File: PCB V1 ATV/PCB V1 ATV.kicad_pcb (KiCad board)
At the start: 2 copper layers, 101.6 x 53.3 mm, 25 parts, among them J1 Power, J10 NW Sensor, J11 N Sensor, J12 NE Sensor, J13 SW Sensor, J14 S Sensor, J15 SE Sensor, J16 Joystick, J17 MotorControl, J2 PWM, J3 Analog, J4 PWM, J5 Analog, J6 Communication, J7 Digital, J8 Battery 12vIN, J9 Motor Controller, SW1 EStop, U1 L7809

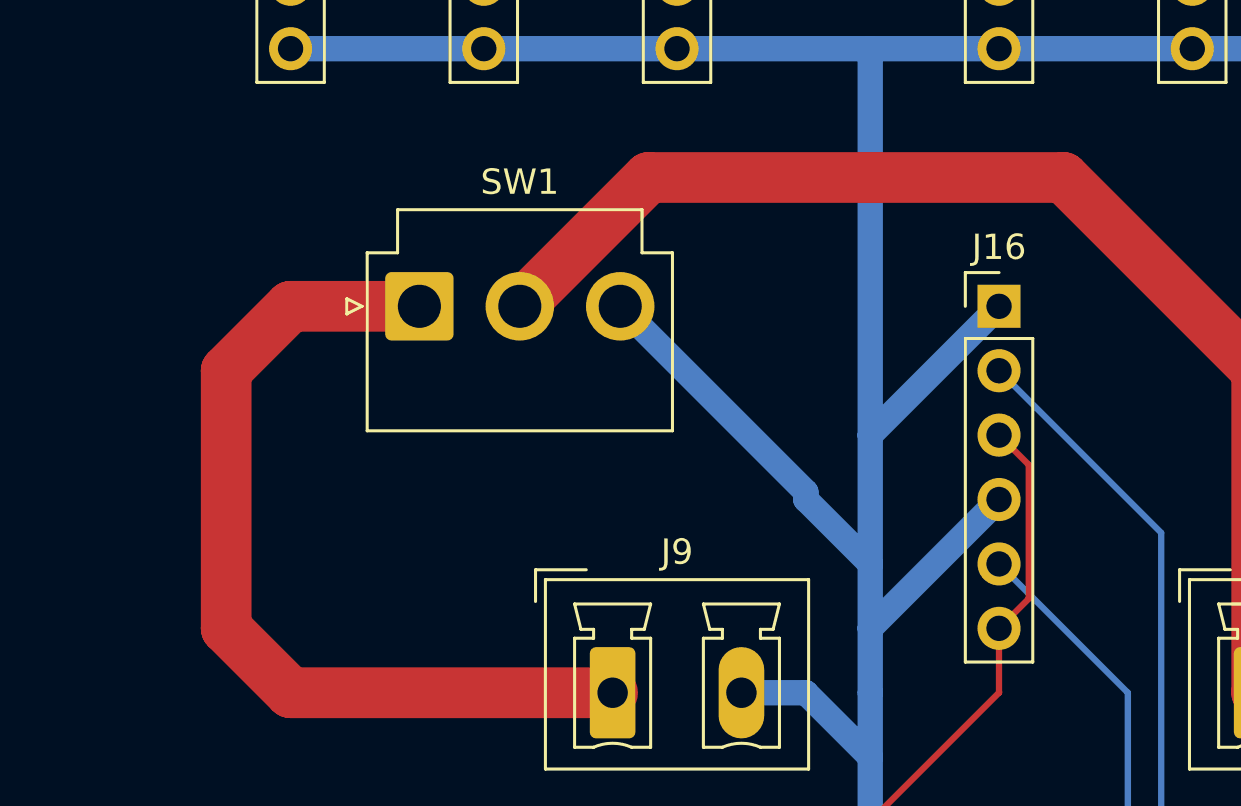
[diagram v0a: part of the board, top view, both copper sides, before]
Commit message: V2.0
Added resistor between estop and ground
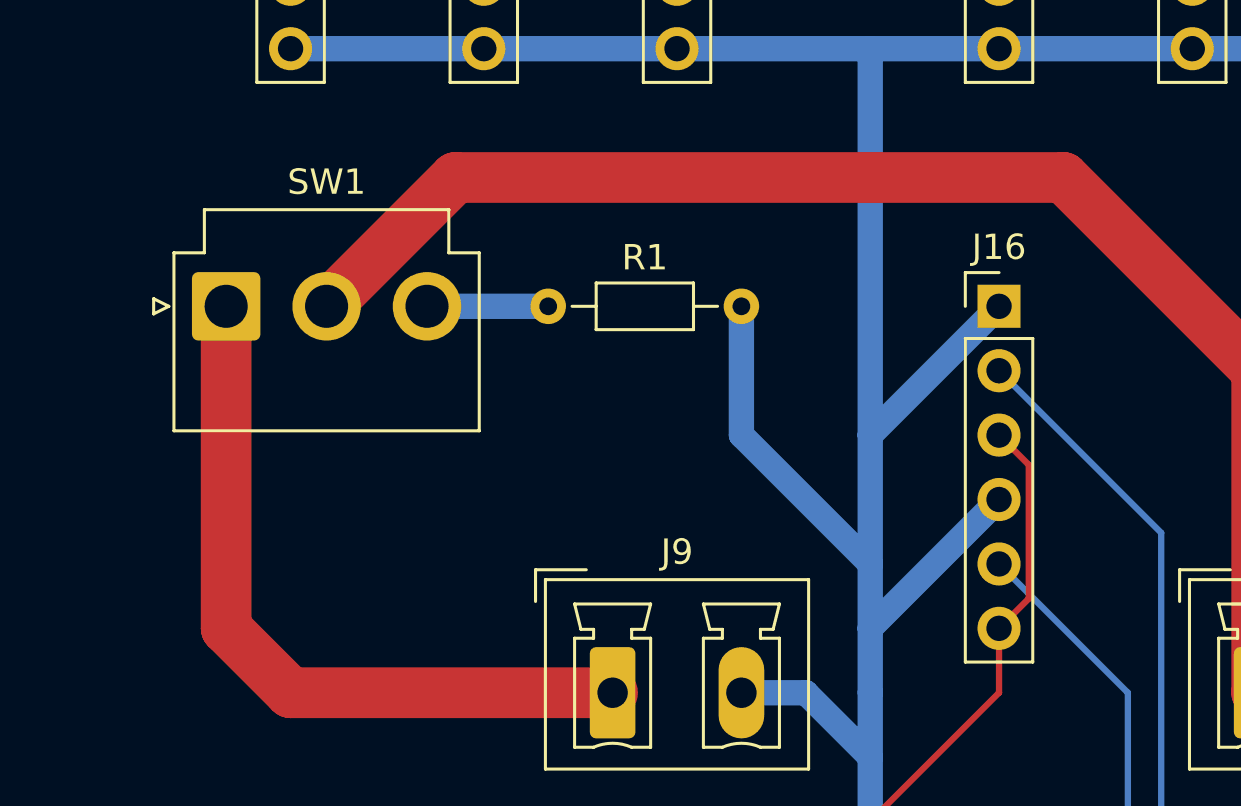
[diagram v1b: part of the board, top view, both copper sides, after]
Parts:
- added R1: R, Resistor_THT:R_Axial_DIN0204_L3.6mm_D1.6mm_P7.62mm_Horizontal, F.Cu at (127.9, 74.6)
- moved SW1 7.62 mm to (115.2, 74.6)
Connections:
- SW1 pad 3: GND -> Net-(SW1A-C)
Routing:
- net Net-(J8-Pin_1): track 70.5 -> 78.1 mm
- net Net-(J9-Pin_1): track 35.1 -> 29.0 mm
- net Net-(SW1A-C): track 0.00 -> 4.78 mm
- net GND: track 162.4 -> 160.4 mm
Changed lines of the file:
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@@
   (net 79 "VCC")
   (net 80 "Net-(J9-Pin_1)")
+  (net 81 "Net-(SW1A-C)")
   (footprint "Connector_PinSocket_2.54mm:PinSocket_2x18_P2.54mm_Vertical" locked (layer "F.Cu")
     (at 193.98 92.38 180)
@@
     (pad "" np_thru_hole circle locked (at 0 0) (size 3.2 3.2) (drill 3.2) (layers "*.Cu" "*.Mask"))
   )
+  (footprint "Resistor_THT:R_Axial_DIN0204_L3.6mm_D1.6mm_P7.62mm_Horizontal" (layer "F.Cu")
+    (at 127.94 74.6)
+    (descr "Resistor, Axial_DIN0204 series, Axial, Horizontal, pin pitch=7.62mm, 0.167W, length*diameter=3.6*1.6mm^2, http://cdn-reichelt.de/documents/datenblatt/B400/1_4W%23YAG.pdf")
+    (tags "Resistor Axial_DIN0204 series Axial Horizontal pin pitch 7.62mm 0.167W length 3.6mm diameter 1.6mm")
+    (property "Sheetfile" "PCB V1 ATV.kicad_sch")
+    (property "Sheetname" "")
+    (property "ki_description" "Resistor")
+    (property "ki_keywords" "R res resistor")
+    (attr through_hole)
+    (fp_text reference "R1" (at 3.81 -1.92) (layer "F.SilkS")
+        (effects (font (size 1 1) (thickness 0.15)))
+    )
+    (fp_text value "R" (at 3.81 1.92) (layer "F.Fab")
+        (effects (font (size 1 1) (thickness 0.15)))
+    )
+    (fp_text user "${REFERENCE}" (at 3.81 0) (layer "F.Fab")
+        (effects (font (size 0.72 0.72) (thickness 0.108)))
+    )
+    (fp_line (start 0.94 0) (end 1.89 0)
+      (stroke (width 0.12) (type solid)) (layer "F.SilkS"))
+    (fp_line (start 1.89 -0.92) (end 1.89 0.92)
+      (stroke (width 0.12) (type solid)) (layer "F.SilkS"))
+    (fp_line (start 1.89 0.92) (end 5.73 0.92)
+      (stroke (width 0.12) (type solid)) (layer "F.SilkS"))
+    (fp_line (start 5.73 -0.92) (end 1.89 -0.92)
+      (stroke (width 0.12) (type solid)) (layer "F.SilkS"))
+    (fp_line (start 5.73 0.92) (end 5.73 -0.92)
+      (stroke (width 0.12) (type solid)) (layer "F.SilkS"))
+    (fp_line (start 6.68 0) (end 5.73 0)
+      (stroke (width 0.12) (type solid)) (layer "F.SilkS"))
+    (fp_line (start -0.95 -1.05) (end -0.95 1.05)
+      (stroke (width 0.05) (type solid)) (layer "F.CrtYd"))
+    (fp_line (start -0.95 1.05) (end 8.57 1.05)
+      (stroke (width 0.05) (type solid)) (layer "F.CrtYd"))
+    (fp_line (start 8.57 -1.05) (end -0.95 -1.05)
+      (stroke (width 0.05) (type solid)) (layer "F.CrtYd"))
+    (fp_line (start 8.57 1.05) (end 8.57 -1.05)
+      (stroke (width 0.05) (type solid)) (layer "F.CrtYd"))
+    (fp_line (start 0 0) (end 2.01 0)
+      (stroke (width 0.1) (type solid)) (layer "F.Fab"))
+    (fp_line (start 2.01 -0.8) (end 2.01 0.8)
+      (stroke (width 0.1) (type solid)) (layer "F.Fab"))
+    (fp_line (start 2.01 0.8) (end 5.61 0.8)
+      (stroke (width 0.1) (type solid)) (layer "F.Fab"))
+    (fp_line (start 5.61 -0.8) (end 2.01 -0.8)
+      (stroke (width 0.1) (type solid)) (layer "F.Fab"))
+    (fp_line (start 5.61 0.8) (end 5.61 -0.8)
+      (stroke (width 0.1) (type solid)) (layer "F.Fab"))
+    (fp_line (start 7.62 0) (end 5.61 0)
+      (stroke (width 0.1) (type solid)) (layer "F.Fab"))
+    (pad "1" thru_hole circle (at 0 0) (size 1.4 1.4) (drill 0.7) (layers "*.Cu" "*.Mask")
+      (net 81 "Net-(SW1A-C)") (pintype "passive"))
+    (pad "2" thru_hole oval (at 7.62 0) (size 1.4 1.4) (drill 0.7) (layers "*.Cu" "*.Mask")
+      (net 1 "GND") (pintype "passive"))
+    (model "${KICAD6_3DMODEL_DIR}/Resistor_THT.3dshapes/R_Axial_DIN0204_L3.6mm_D1.6mm_P7.62mm_Horizontal.wrl"
+      (offset (xyz 0 0 0))
+      (scale (xyz 1 1 1))
+      (rotate (xyz 0 0 0))
+    )
+  )
   (footprint "Connector_Phoenix_MC_HighVoltage:PhoenixContact_MCV_1,5_2-G-5.08_1x02_P5.08mm_Vertical" (layer "F.Cu")
     (at 130.48 89.84)
@@
   )
   (footprint "Connector_JST:JST_VH_B3P-VH-B_1x03_P3.96mm_Vertical" (layer "F.Cu")
-    (at 122.86 74.6)
+    (at 115.24 74.6)
     (descr "JST VH PBT series connector, B3P-VH-B (http://www.jst-mfg.com/product/pdf/eng/eVH.pdf), generated with kicad-footprint-generator")
     (tags "connector JST VH vertical")
@@
       (net 78 "Net-(J8-Pin_1)") (pinfunction "B") (pintype "passive"))
     (pad "3" thru_hole circle (at 7.92 0) (size 2.7 2.7) (drill 1.7) (layers "*.Cu" "*.Mask")
-      (net 1 "GND") (pinfunction "C") (pintype "passive"))
+      (net 81 "Net-(SW1A-C)") (pinfunction "C") (pintype "passive"))
     (model "${KICAD6_3DMODEL_DIR}/Connector_JST.3dshapes/JST_VH_B3P-VH-B_1x03_P3.96mm_Vertical.wrl"
       (offset (xyz 0 0 0))
@@
   (segment (start 140.64 89.84) (end 140.64 97.46) (width 1) (layer "B.Cu") (net 1))
   (segment (start 158.42 84.76) (end 160.96 87.3) (width 1) (layer "B.Cu") (net 1))
-  (segment (start 138.1 82.22) (end 138.1 81.92) (width 1) (layer "B.Cu") (net 1))
   (segment (start 193.98 92.38) (end 196.52 92.38) (width 1) (layer "B.Cu") (net 1))
-  (segment (start 138.1 81.92) (end 130.78 74.6) (width 1) (layer "B.Cu") (net 1))
+  (segment (start 135.56 74.6) (end 135.56 79.68) (width 1) (layer "B.Cu") (net 1))
   (segment (start 140.64 84.76) (end 140.64 79.68) (width 1) (layer "B.Cu") (net 1))
   (segment (start 140.64 89.84) (end 140.64 87.3) (width 1) (layer "B.Cu") (net 1))
@@
   (segment (start 140.64 79.68) (end 140.64 64.44) (width 1) (layer "B.Cu") (net 1))
   (segment (start 145.72 64.44) (end 153.34 64.44) (width 1) (layer "B.Cu") (net 1))
+  (segment (start 135.56 79.68) (end 140.64 84.76) (width 1) (layer "B.Cu") (net 1))
   (segment (start 158.42 64.44) (end 158.42 84.76) (width 1) (layer "B.Cu") (net 1))
   (segment (start 140.64 87.3) (end 145.72 82.22) (width 1) (layer "B.Cu") (net 1))
@@
   (segment (start 178.74 82.22) (end 178.74 87.3) (width 1) (layer "B.Cu") (net 1))
   (segment (start 140.64 79.68) (end 145.72 74.6) (width 1) (layer "B.Cu") (net 1))
-  (segment (start 138.1 82.22) (end 140.64 84.76) (width 1) (layer "B.Cu") (net 1))
   (segment (start 158.42 64.44) (end 160.96 64.44) (width 1) (layer "B.Cu") (net 1))
   (segment (start 117.78 64.44) (end 125.4 64.44) (width 1) (layer "B.Cu") (net 1))
@@
   (segment (start 163.5 59.36) (end 163.5 54.28) (width 0.25) (layer "B.Cu") (net 64))
   (segment (start 155.88 89.84) (end 163.5 82.22) (width 2) (layer "F.Cu") (net 78))
-  (segment (start 148.26 69.52) (end 131.9 69.52) (width 2) (layer "F.Cu") (net 78))
+  (segment (start 155.88 89.84) (end 155.88 77.14) (width 2) (layer "F.Cu") (net 78))
+  (segment (start 124.28 69.52) (end 119.2 74.6) (width 2) (layer "F.Cu") (net 78))
+  (segment (start 148.26 69.52) (end 124.28 69.52) (width 2) (layer "F.Cu") (net 78))
   (segment (start 155.88 77.14) (end 148.26 69.52) (width 2) (layer "F.Cu") (net 78))
-  (segment (start 155.88 89.84) (end 155.88 77.14) (width 2) (layer "F.Cu") (net 78))
-  (segment (start 131.9 69.52) (end 126.82 74.6) (width 2) (layer "F.Cu") (net 78))
   (segment (start 163.5 82.22) (end 176.2 82.22) (width 2) (layer "F.Cu") (net 78))
   (segment (start 181.28 92.38) (end 181.28 82.22) (width 1) (layer "F.Cu") (net 79))
@@
   (segment (start 145.72 97.46) (end 148.26 94.92) (width 1) (layer "F.Cu") (net 79))
   (segment (start 178.74 94.92) (end 181.28 92.38) (width 1) (layer "F.Cu") (net 79))
+  (segment (start 115.24 74.6) (end 115.24 87.3) (width 2) (layer "F.Cu") (net 80))
+  (segment (start 117.78 89.84) (end 130.48 89.84) (width 2) (layer "F.Cu") (net 80))
   (segment (start 115.24 87.3) (end 117.78 89.84) (width 2) (layer "F.Cu") (net 80))
-  (segment (start 115.24 77.14) (end 115.24 87.3) (width 2) (layer "F.Cu") (net 80))
-  (segment (start 117.78 89.84) (end 130.48 89.84) (width 2) (layer "F.Cu") (net 80))
-  (segment (start 117.78 74.6) (end 115.24 77.14) (width 2) (layer "F.Cu") (net 80))
-  (segment (start 122.86 74.6) (end 117.78 74.6) (width 2) (layer "F.Cu") (net 80))
+  (segment (start 127.94 74.6) (end 123.16 74.6) (width 1) (layer "B.Cu") (net 81))
 )

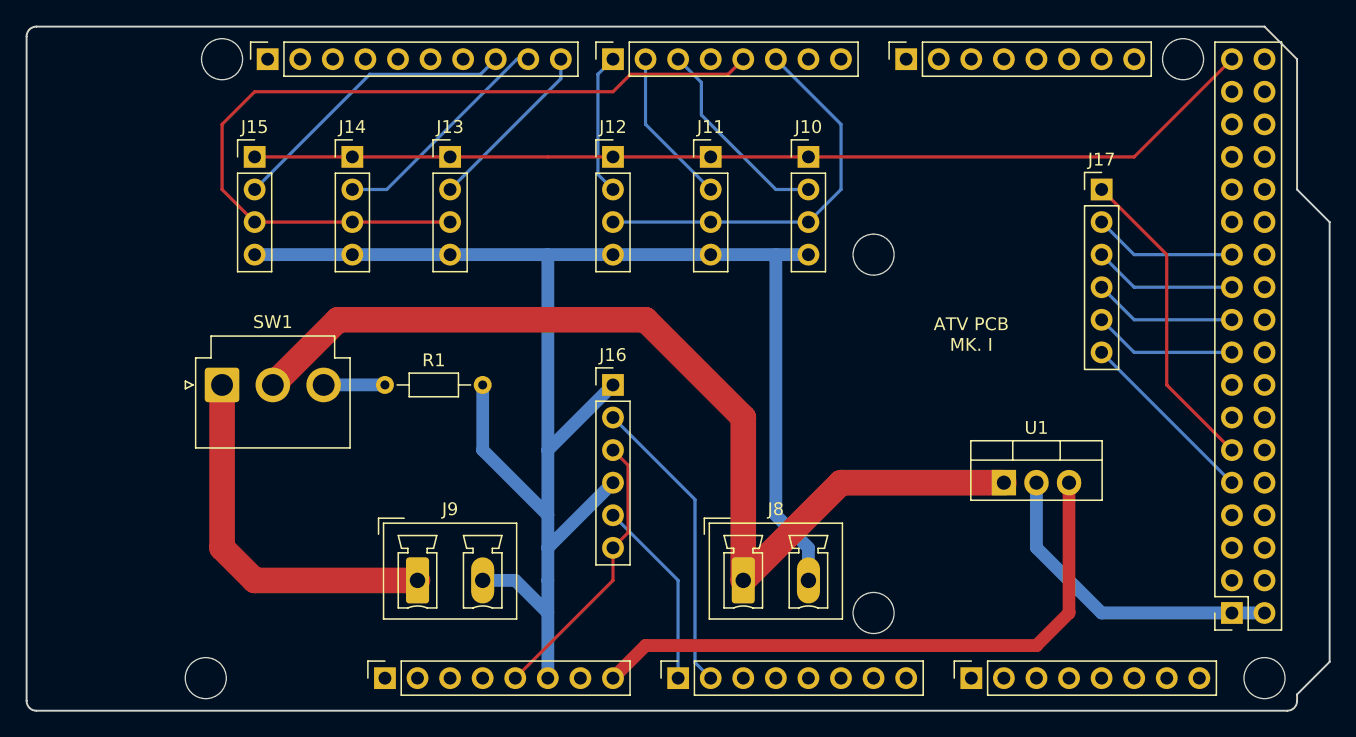
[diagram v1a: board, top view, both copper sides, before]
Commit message: V1.2
Updated the board to fit the 2 part phoenix connectors, added a resistor, and added more silkscreen. Also removed .gbr and .drl files
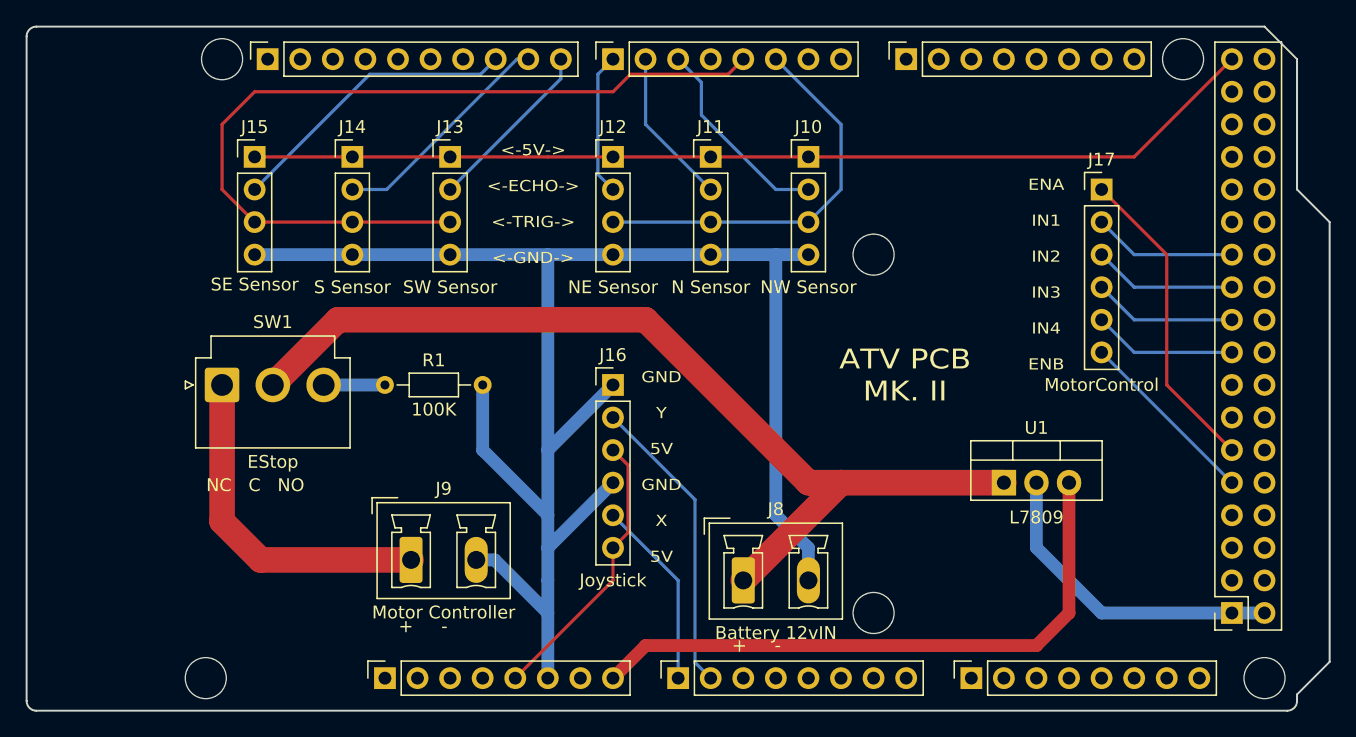
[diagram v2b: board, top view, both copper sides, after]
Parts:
- J8, J9: footprint Connector_Phoenix_MC_HighVoltage:PhoenixContact_MCV_1,5_2-G-5.08_1x02_P5.08mm_Vertical -> Custom:Custom 2 Part Phoenix Connector
- R1: value R -> 100K
- moved J9 1.67 mm to (130.0, 88.2)
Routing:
- net Net-(J8-Pin_1): track 78.1 -> 75.1 mm
- net Net-(J9-Pin_1): track 29.0 -> 26.6 mm
- net GND: track 160.4 -> 161.5 mm
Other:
- board text added: "+ -"
- board text added: "<-5V-> <-ECHO-> <-TRIG-> <-GND->"
- board text added: "ATV PCB MK. II"
- board text added: "ENA IN1 IN2 IN3 IN4 ENB"
- board text added: "GND Y 5V GND X 5V"
- board text added: "NC C NO"
- board text removed: "ATV PCB MK. I"
